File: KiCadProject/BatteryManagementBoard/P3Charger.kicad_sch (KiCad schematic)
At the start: 58 parts, among them Q301 NFET_Gatenames, Q302 NFET_Gatenames, Q303 NFET_Gatenames, Q304 NFET_Gatenames, Q305 PMOS_Gatenames, U301 BQ25713

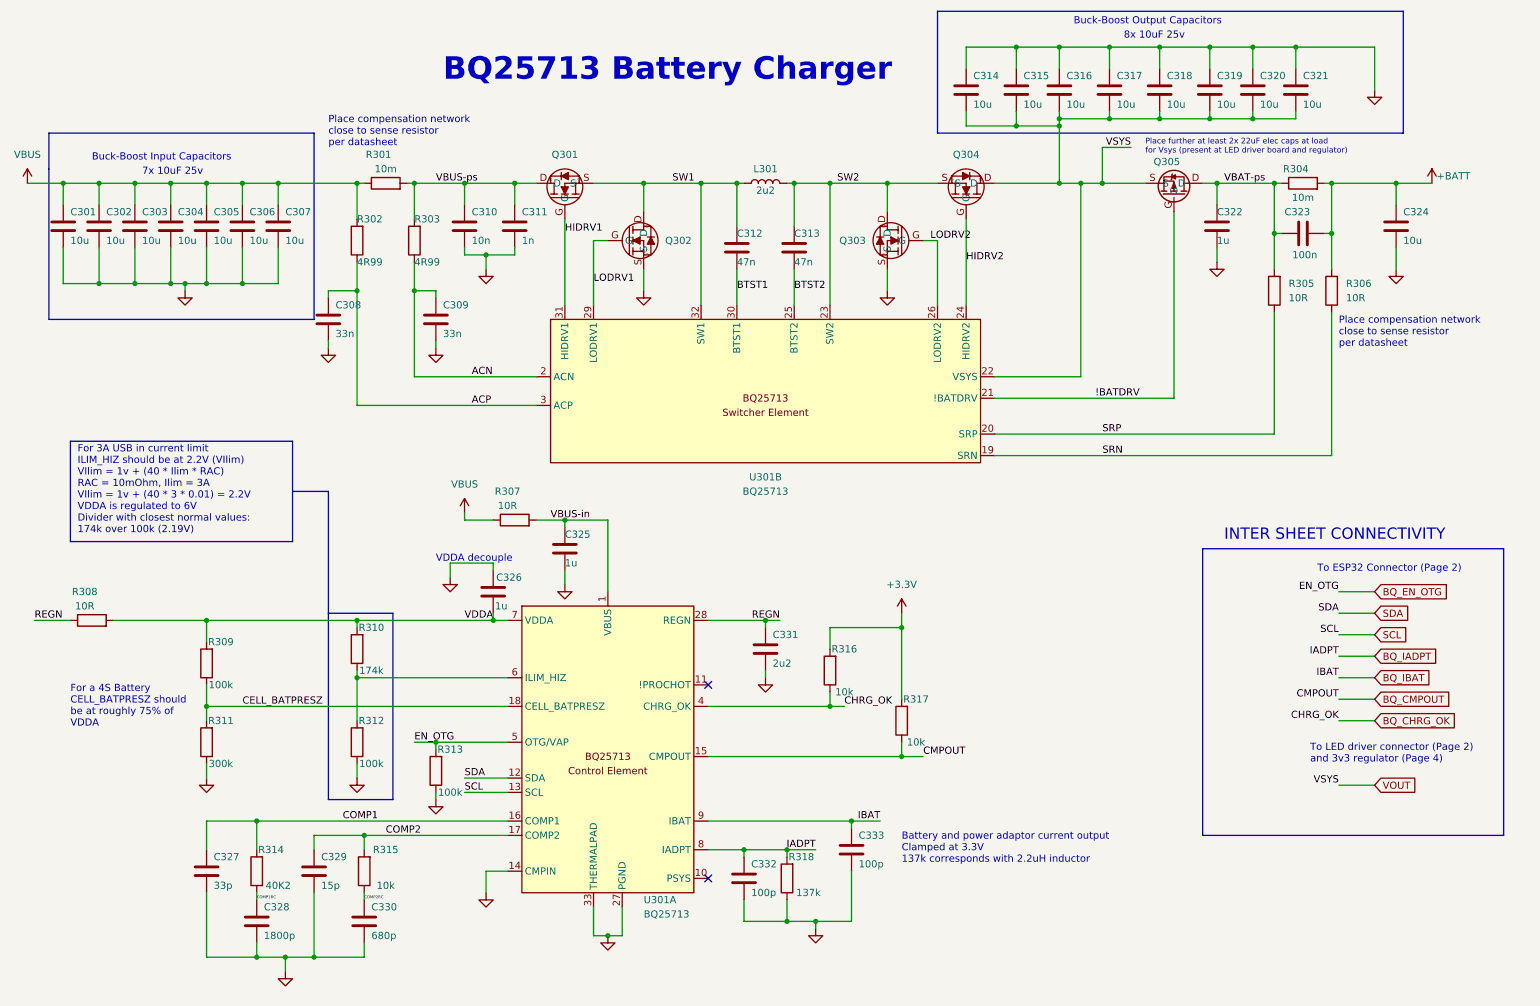
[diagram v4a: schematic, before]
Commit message: ESP board layout mostly done. Small updates to battery management board
Signed-off-by: Eldalote.Electronics <Eldalote.Electronics@gmail.com>
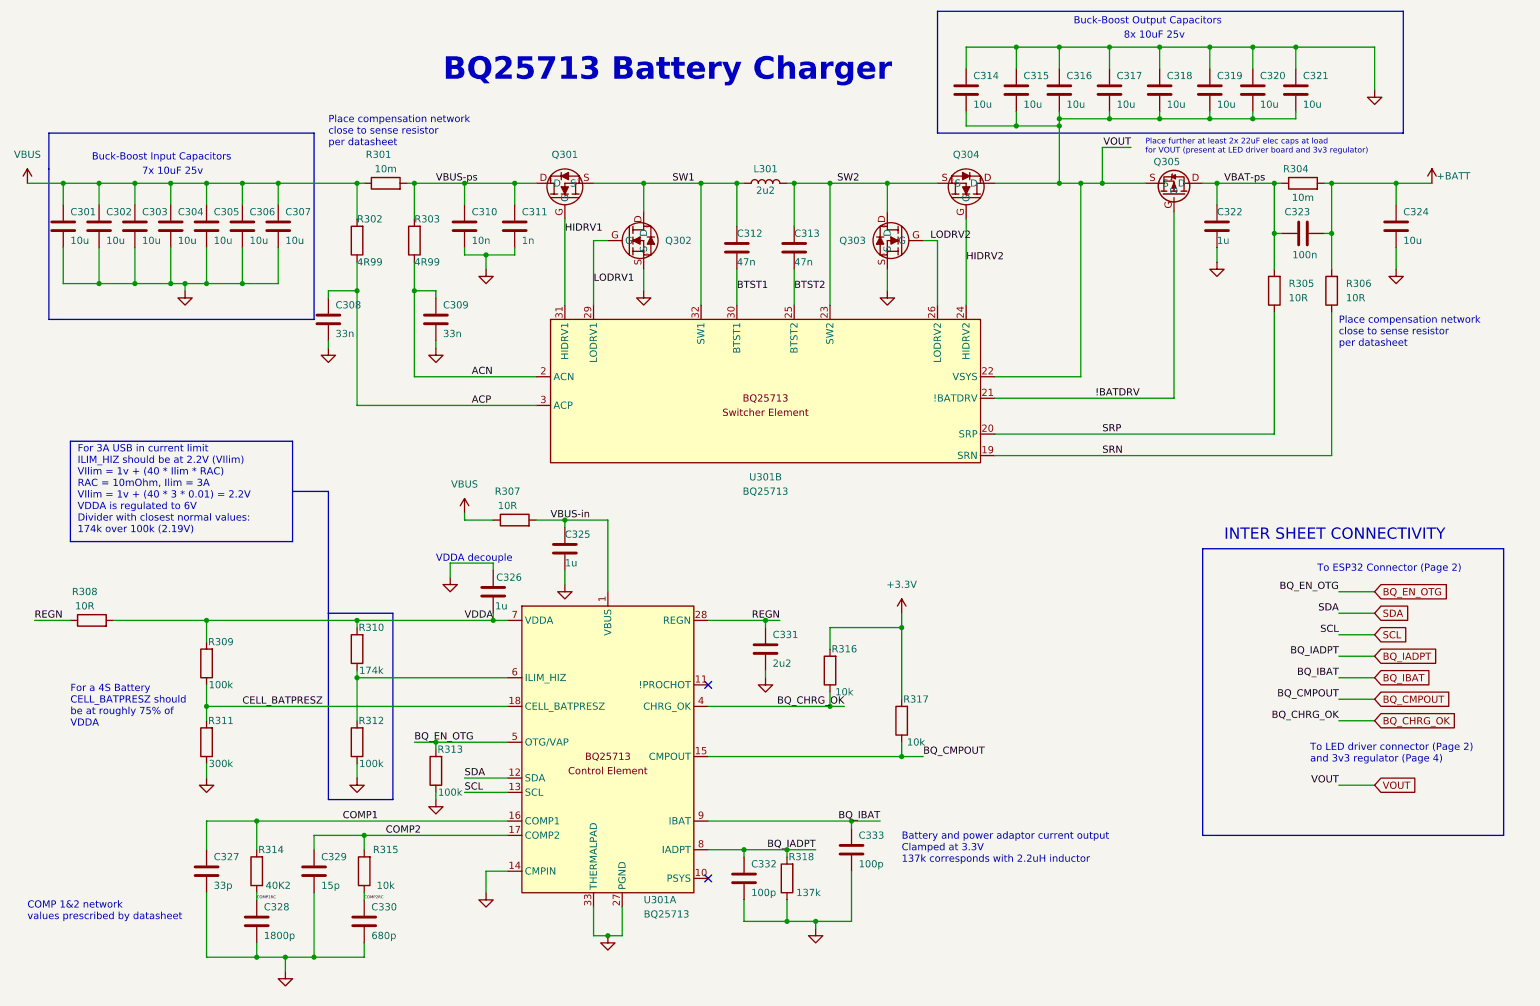
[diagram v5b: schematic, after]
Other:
- note added: "COMP 1&2 network values prescribed by datasheet"
- note added: "Place further at least 2x 22uF elec caps at load for VOUT (present at LED driver board and 3v3 regulator)"
- note removed: "Place further at least 2x 22uF elec caps at load for Vsys (present at LED driver board and regulator)"
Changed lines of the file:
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@@
     (effects (font (size 1.27 1.27)) (justify left bottom))
   )
-  (text "Place further at least 2x 22uF elec caps at load\nfor Vsys (present at LED driver board and regulator)"
+  (text "COMP 1&2 network\nvalues prescribed by datasheet\n" (at 17.78 173.99 0)
+    (effects (font (size 1.27 1.27)) (justify left bottom))
+  )
+  (text "Place further at least 2x 22uF elec caps at load\nfor VOUT (present at LED driver board and 3v3 regulator)"
     (at 215.9 38.1 0)
     (effects (font (size 1 1)) (justify left bottom))
@@
     (effects (font (size 1.27 1.27)) (justify right bottom))
   )
-  (label "VSYS" (at 213.36 36.83 180)
+  (label "VOUT" (at 213.36 36.83 180)
     (effects (font (size 1.27 1.27)) (justify right bottom))
   )
@@
     (effects (font (size 1.27 1.27)) (justify right bottom))
   )
-  (label "CMPOUT" (at 250.19 134.62 180)
+  (label "BQ_CMPOUT" (at 250.19 134.62 180)
     (effects (font (size 1.27 1.27)) (justify right bottom))
   )
@@
     (effects (font (size 1.27 1.27)) (justify left bottom))
   )
-  (label "IADPT" (at 250.19 127 180)
+  (label "BQ_IADPT" (at 250.19 127 180)
     (effects (font (size 1.27 1.27)) (justify right bottom))
   )
@@
     (effects (font (size 1.27 1.27)) (justify left bottom))
   )
-  (label "IADPT" (at 157.48 161.29 180)
+  (label "BQ_IADPT" (at 157.48 161.29 180)
     (effects (font (size 1.27 1.27)) (justify right bottom))
   )
-  (label "EN_OTG" (at 250.19 115.57 180)
+  (label "BQ_EN_OTG" (at 250.19 115.57 180)
     (effects (font (size 1.27 1.27)) (justify right bottom))
   )
-  (label "CHRG_OK" (at 250.19 138.43 180)
+  (label "BQ_CHRG_OK" (at 250.19 138.43 180)
     (effects (font (size 1.27 1.27)) (justify right bottom))
   )
-  (label "VSYS" (at 250.19 149.86 180)
+  (label "VOUT" (at 250.19 149.86 180)
     (effects (font (size 1.27 1.27)) (justify right bottom))
   )
@@
     (effects (font (size 1.27 1.27)) (justify left bottom))
   )
-  (label "CMPOUT" (at 176.53 144.78 0)
+  (label "BQ_CMPOUT" (at 176.53 144.78 0)
     (effects (font (size 1.27 1.27)) (justify left bottom))
   )
-  (label "IBAT" (at 250.19 130.81 180)
+  (label "BQ_IBAT" (at 250.19 130.81 180)
     (effects (font (size 1.27 1.27)) (justify right bottom))
   )
@@
     (effects (font (size 1.27 1.27)) (justify left bottom))
   )
-  (label "EN_OTG" (at 86.36 142.24 0)
+  (label "BQ_EN_OTG" (at 86.36 142.24 0)
     (effects (font (size 1.27 1.27)) (justify left bottom))
   )
@@
     (effects (font (size 1.27 1.27)) (justify left bottom))
   )
-  (label "CHRG_OK" (at 162.56 135.89 0)
-    (effects (font (size 1.27 1.27)) (justify left bottom))
-  )
-  (label "IBAT" (at 168.91 156.21 180)
+  (label "BQ_CHRG_OK" (at 162.56 135.89 180)
     (effects (font (size 1.27 1.27)) (justify right bottom))
   )
+  (label "BQ_IBAT" (at 168.91 156.21 180)
+    (effects (font (size 1.27 1.27)) (justify right bottom))
+  )

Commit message: Tweaking
Signed-off-by: Eldalote.Electronics <Eldalote.Electronics@gmail.com>
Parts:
- R301, R304: footprint (none) -> Resistor_SMD:R_1206_3216Metric
- R302, R303, R305, R306, R307, R308, R309, R310, R311, R312, R313, R314, R315, R316, R317, R318: footprint (none) -> Resistor_SMD:R_0402_1005Metric
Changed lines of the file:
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@@
   (junction (at 113.03 102.87) (diameter 0) (color 0 0 0 0)
+  )
+  (junction (at 210.82 43.18) (diameter 0) (color 0 0 0 0)
   )
   (junction (at 76.2 120.65) (diameter 0) (color 0 0 0 0)
@@
     (stroke (width 0) (type default) (color 0 0 0 0))
   )
+  (wire (pts (xy 210.82 43.18) (xy 215.9 43.18))
+    (stroke (width 0) (type default) (color 0 0 0 0))
+  )
   (wire (pts (xy 58.42 168.91) (xy 58.42 170.18))
     (stroke (width 0) (type default) (color 0 0 0 0))
@@
     (stroke (width 0) (type default) (color 0 0 0 0))
   )
-  (wire (pts (xy 208.28 43.18) (xy 215.9 43.18))
+  (wire (pts (xy 208.28 43.18) (xy 210.82 43.18))
     (stroke (width 0) (type default) (color 0 0 0 0))
   )
@@
     (property "Reference" "R308" (id 0) (at 27.94 115.57 90))
     (property "Value" "10R" (id 1) (at 27.94 118.11 90))
-    (property "Footprint" "" (id 2) (at 29.21 122.428 90)
+    (property "Footprint" "Resistor_SMD:R_0402_1005Metric" (id 2) (at 29.21 122.428 90)
       (effects (font (size 1.27 1.27)) hide)
     )
@@
     (property "Reference" "R318" (id 0) (at 154.94 162.56 0))
     (property "Value" "137k" (id 1) (at 156.21 168.91 0))
-    (property "Footprint" "" (id 2) (at 154.178 166.37 90)
+    (property "Footprint" "Resistor_SMD:R_0402_1005Metric" (id 2) (at 154.178 166.37 90)
       (effects (font (size 1.27 1.27)) hide)
     )
@@
     (property "Reference" "R313" (id 0) (at 92.71 143.51 0))
     (property "Value" "100k" (id 1) (at 92.71 151.13 0))
-    (property "Footprint" "" (id 2) (at 91.948 147.32 90)
+    (property "Footprint" "Resistor_SMD:R_0402_1005Metric" (id 2) (at 91.948 147.32 90)
       (effects (font (size 1.27 1.27)) hide)
     )
@@
     (property "Reference" "R312" (id 0) (at 78.74 138.43 0))
     (property "Value" "100k" (id 1) (at 78.74 146.05 0))
-    (property "Footprint" "" (id 2) (at 77.978 142.24 90)
+    (property "Footprint" "Resistor_SMD:R_0402_1005Metric" (id 2) (at 77.978 142.24 90)
       (effects (font (size 1.27 1.27)) hide)
     )
@@
     (property "Reference" "R304" (id 0) (at 242.57 40.64 90))
     (property "Value" "10m" (id 1) (at 243.84 45.72 90))
-    (property "Footprint" "" (id 2) (at 243.84 44.958 90)
+    (property "Footprint" "Resistor_SMD:R_1206_3216Metric" (id 2) (at 243.84 44.958 90)
       (effects (font (size 1.27 1.27)) hide)
     )
@@
     (property "Reference" "R307" (id 0) (at 102.87 97.79 90))
     (property "Value" "10R" (id 1) (at 102.87 100.33 90))
-    (property "Footprint" "" (id 2) (at 104.14 104.648 90)
+    (property "Footprint" "Resistor_SMD:R_0402_1005Metric" (id 2) (at 104.14 104.648 90)
       (effects (font (size 1.27 1.27)) hide)
     )
@@
     (pin "1")
     (pin "2")
+  )
+  (symbol (lib_id "power:PWR_FLAG") (at 210.82 43.18 0) (unit 1)
+    (in_bom yes) (on_board yes)
+    (property "Reference" "#FLG0101" (id 0) (at 210.82 41.275 0)
+      (effects (font (size 1.27 1.27)) hide)
+    )
+    (property "Value" "PWR_FLAG" (id 1) (at 210.82 39.37 0)
+      (effects (font (size 1.27 1.27)) hide)
+    )
+    (property "Footprint" "" (id 2) (at 210.82 43.18 0)
+      (effects (font (size 1.27 1.27)) hide)
+    )
+    (property "Datasheet" "~" (id 3) (at 210.82 43.18 0)
+      (effects (font (size 1.27 1.27)) hide)
+    )
+    (pin "1")
   )
   (symbol (lib_id "Eldalote_symbols:BQ25713") (at 120.65 143.51 0) (unit 1)
@@
       (effects (font (size 1.27 1.27)) (justify right))
     )
-    (property "Footprint" "" (id 2) (at 88.138 53.34 90)
+    (property "Footprint" "Resistor_SMD:R_0402_1005Metric" (id 2) (at 88.138 53.34 90)
       (effects (font (size 1.27 1.27)) hide)
     )
@@
     (property "Reference" "R311" (id 0) (at 52.07 138.43 0))
     (property "Value" "300k" (id 1) (at 52.07 146.05 0))
-    (property "Footprint" "" (id 2) (at 51.308 142.24 90)
+    (property "Footprint" "Resistor_SMD:R_0402_1005Metric" (id 2) (at 51.308 142.24 90)
       (effects (font (size 1.27 1.27)) hide)
     )
@@
     (property "Reference" "R309" (id 0) (at 52.07 124.46 0))
     (property "Value" "100k" (id 1) (at 52.07 132.08 0))
-    (property "Footprint" "" (id 2) (at 51.308 128.27 90)
+    (property "Footprint" "Resistor_SMD:R_0402_1005Metric" (id 2) (at 51.308 128.27 90)
       (effects (font (size 1.27 1.27)) hide)
     )
@@
     (property "Reference" "R315" (id 0) (at 81.28 161.29 0))
     (property "Value" "10k" (id 1) (at 81.28 167.64 0))
-    (property "Footprint" "" (id 2) (at 79.248 165.1 90)
+    (property "Footprint" "Resistor_SMD:R_0402_1005Metric" (id 2) (at 79.248 165.1 90)
       (effects (font (size 1.27 1.27)) hide)
     )
@@
     (property "Reference" "R310" (id 0) (at 78.74 121.92 0))
     (property "Value" "174k" (id 1) (at 78.74 129.54 0))
-    (property "Footprint" "" (id 2) (at 77.978 125.73 90)
+    (property "Footprint" "Resistor_SMD:R_0402_1005Metric" (id 2) (at 77.978 125.73 90)
       (effects (font (size 1.27 1.27)) hide)
     )
@@
       (effects (font (size 1.27 1.27)) (justify right))
     )
-    (property "Footprint" "" (id 2) (at 250.698 62.23 90)
+    (property "Footprint" "Resistor_SMD:R_0402_1005Metric" (id 2) (at 250.698 62.23 90)
       (effects (font (size 1.27 1.27)) hide)
     )
@@
     (property "Reference" "R314" (id 0) (at 60.96 161.29 0))
     (property "Value" "40K2" (id 1) (at 62.23 167.64 0))
-    (property "Footprint" "" (id 2) (at 60.198 165.1 90)
+    (property "Footprint" "Resistor_SMD:R_0402_1005Metric" (id 2) (at 60.198 165.1 90)
       (effects (font (size 1.27 1.27)) hide)
     )
@@
     (property "Reference" "R317" (id 0) (at 175.26 134.62 0))
     (property "Value" "10k" (id 1) (at 175.26 142.24 0))
-    (property "Footprint" "" (id 2) (at 174.498 138.43 90)
+    (property "Footprint" "Resistor_SMD:R_0402_1005Metric" (id 2) (at 174.498 138.43 90)
       (effects (font (size 1.27 1.27)) hide)
     )
@@
       (effects (font (size 1.27 1.27)) (justify right))
     )
-    (property "Footprint" "" (id 2) (at 77.978 53.34 90)
+    (property "Footprint" "Resistor_SMD:R_0402_1005Metric" (id 2) (at 77.978 53.34 90)
       (effects (font (size 1.27 1.27)) hide)
     )
@@
     (property "Reference" "R316" (id 0) (at 162.56 125.73 0))
     (property "Value" "10k" (id 1) (at 162.56 133.35 0))
-    (property "Footprint" "" (id 2) (at 161.798 129.54 90)
+    (property "Footprint" "Resistor_SMD:R_0402_1005Metric" (id 2) (at 161.798 129.54 90)
       (effects (font (size 1.27 1.27)) hide)
     )
@@
     (property "Reference" "R301" (id 0) (at 80.01 38.1 90))
     (property "Value" "10m" (id 1) (at 81.28 40.64 90))
-    (property "Footprint" "" (id 2) (at 81.28 44.958 90)
+    (property "Footprint" "Resistor_SMD:R_1206_3216Metric" (id 2) (at 81.28 44.958 90)
       (effects (font (size 1.27 1.27)) hide)
     )
@@
     (pin "2")
   )
-  (symbol (lib_name "BQ25713_1") (lib_id "Eldalote_symbols:BQ25713") (at 148.59 80.01 0) (unit 2)
+  (symbol (lib_id "Eldalote_symbols:BQ25713") (at 148.59 80.01 0) (unit 2)
     (in_bom yes) (on_board yes) (fields_autoplaced)
     (property "Reference" "U301" (id 0) (at 148.59 95.25 0))
@@
       (effects (font (size 1.27 1.27)) (justify right))
     )
-    (property "Footprint" "" (id 2) (at 240.538 62.23 90)
-      (effects (font (size 1.27 1.27)) hide)
-    )
+    (property "Footprint" "Resistor_SMD:R_0402_1005Metric" (id 2) (at 240.538 62.23 90)
+      (effects (font (size 1.27 1.27)) hide)
+    )

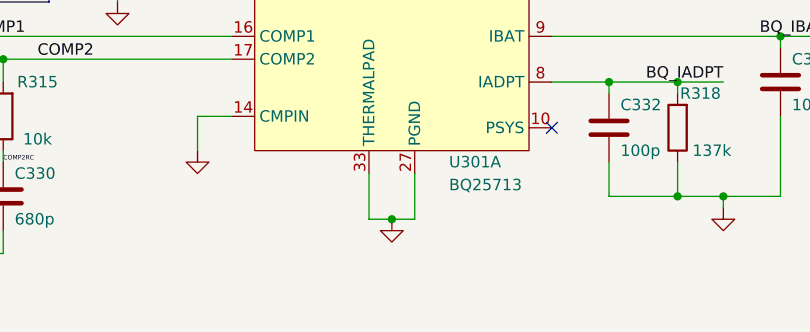
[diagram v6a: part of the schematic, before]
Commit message: Final touches before component order and PCB layout
Signed-off-by: Eldalote.Electronics <Eldalote.Electronics@gmail.com>
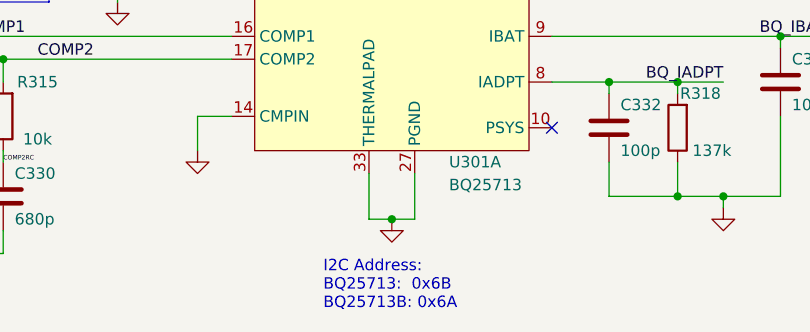
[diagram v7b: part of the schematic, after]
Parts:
- L301: footprint (none) -> Eldalote-footprints:SRP-1265C
- Q301, Q302, Q303, Q304: footprint (none) -> Eldalote-footprints:SSM6K504
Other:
- note added: "I2C Address: BQ25713: 0x6B BQ25713B: 0x6A"
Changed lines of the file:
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@@
+    (effects (font (size 1.27 1.27)) (justify left bottom))
+  )
+  (text "I2C Address: \nBQ25713:  0x6B\nBQ25713B: 0x6A" (at 113.03 186.69 0)
     (effects (font (size 1.27 1.27)) (justify left bottom))
   )
@@
       (effects (font (size 1.27 1.27)) hide)
     )
-    (property "Footprint" "" (id 2) (at 113.03 43.18 0)
+    (property "Footprint" "Eldalote-footprints:SSM6K504" (id 2) (at 113.03 43.18 0)
       (effects (font (size 1.27 1.27)) hide)
     )
@@
     (property "Reference" "L301" (id 0) (at 148.59 40.64 90))
     (property "Value" "2u2" (id 1) (at 148.59 44.45 90))
-    (property "Footprint" "" (id 2) (at 148.59 43.18 0)
+    (property "Footprint" "Eldalote-footprints:SRP-1265C" (id 2) (at 148.59 43.18 0)
       (effects (font (size 1.27 1.27)) hide)
     )
@@
       (effects (font (size 1.27 1.27)) hide)
     )
-    (property "Footprint" "" (id 2) (at 170.18 53.34 0)
+    (property "Footprint" "Eldalote-footprints:SSM6K504" (id 2) (at 170.18 53.34 0)
       (effects (font (size 1.27 1.27)) hide)
     )
@@
       (effects (font (size 1.27 1.27)) hide)
     )
-    (property "Footprint" "" (id 2) (at 127 53.34 0)
+    (property "Footprint" "Eldalote-footprints:SSM6K504" (id 2) (at 127 53.34 0)
       (effects (font (size 1.27 1.27)) hide)
     )
@@
       (effects (font (size 1.27 1.27)) hide)
     )
-    (property "Footprint" "" (id 2) (at 184.15 43.18 0)
-      (effects (font (size 1.27 1.27)) hide)
-    )
+    (property "Footprint" "Eldalote-footprints:SSM6K504" (id 2) (at 184.15 43.18 0)
+      (effects (font (size 1.27 1.27)) hide)
+    )

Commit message: Final tweaks before component order and PCB completion mk2
Signed-off-by: Eldalote.Electronics <Eldalote.Electronics@gmail.com>
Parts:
- Q301, Q302, Q303, Q304: footprint Eldalote-footprints:SSM6K504 -> Eldalote-footprints:DFN3x3A_8L_EP1_P
- Q305: footprint (none) -> Eldalote-footprints:DFN3x3A_8L_EP1_P
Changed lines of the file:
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@@
       (effects (font (size 1.27 1.27)) hide)
     )
-    (property "Footprint" "Eldalote-footprints:SSM6K504" (id 2) (at 113.03 43.18 0)
+    (property "Footprint" "Eldalote-footprints:DFN3x3A_8L_EP1_P" (id 2) (at 113.03 43.18 0)
       (effects (font (size 1.27 1.27)) hide)
     )
@@
       (effects (font (size 1.27 1.27)) hide)
     )
-    (property "Footprint" "Eldalote-footprints:SSM6K504" (id 2) (at 170.18 53.34 0)
+    (property "Footprint" "Eldalote-footprints:DFN3x3A_8L_EP1_P" (id 2) (at 170.18 53.34 0)
       (effects (font (size 1.27 1.27)) hide)
     )
@@
       (effects (font (size 1.27 1.27)) hide)
     )
-    (property "Footprint" "Eldalote-footprints:SSM6K504" (id 2) (at 127 53.34 0)
+    (property "Footprint" "Eldalote-footprints:DFN3x3A_8L_EP1_P" (id 2) (at 127 53.34 0)
       (effects (font (size 1.27 1.27)) hide)
     )
@@
       (effects (font (size 1.27 1.27)) hide)
     )
-    (property "Footprint" "" (id 2) (at 220.98 43.18 0)
+    (property "Footprint" "Eldalote-footprints:DFN3x3A_8L_EP1_P" (id 2) (at 220.98 43.18 0)
       (effects (font (size 1.27 1.27)) hide)
     )
@@
       (effects (font (size 1.27 1.27)) hide)
     )
-    (property "Footprint" "Eldalote-footprints:SSM6K504" (id 2) (at 184.15 43.18 0)
-      (effects (font (size 1.27 1.27)) hide)
-    )
+    (property "Footprint" "Eldalote-footprints:DFN3x3A_8L_EP1_P" (id 2) (at 184.15 43.18 0)
+      (effects (font (size 1.27 1.27)) hide)
+    )
